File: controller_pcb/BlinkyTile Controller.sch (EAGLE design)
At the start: 29 parts, among them CON1 USB_MICROSMT+THRUHULE, Q1 16MHz, U1 MK20D--VFM5, U2 W25Q--DVSS(208), U3 74LVC1G17DCK, U4 74LVC1G17DCK, U5 74LVC1G17DCK, U6 TPD4S012

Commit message: Add protection diode, JST battery connector, tweak positions for manufacturability, redo silk
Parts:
- added CN1: (no value), adafruit:JST_2PIN-THM-RA
- added D1: (no value), adafruit:DIODESOD-323F
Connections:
- new net N$9: D1.A, L3.P$1
- net +5V: now also CN1.2, D1.C; no longer L3.P$1
- net GND: now also CN1.1
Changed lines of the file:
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@@
 <part name="L3" library="blinkinlabs" deviceset="FB" device="0805/NO-OUTLINE" value="130ohm @100MHz"/>
 <part name="L2" library="blinkinlabs" deviceset="FB" device="0805/NO-OUTLINE" value="130ohm @100MHz"/>
+<part name="CN1" library="adafruit" deviceset="JST_2PIN" device="-THM-RA"/>
+<part name="P+5" library="supply1" deviceset="+5V" device=""/>
+<part name="GND6" library="supply1" deviceset="GND" device=""/>
+<part name="D1" library="adafruit" deviceset="DIODE" device="SOD-323F"/>
 </parts>
 <sheets>
@@
 <instance part="L3" gate="G$1" x="78.74" y="195.58"/>
 <instance part="L2" gate="G$1" x="43.18" y="172.72" rot="R90"/>
+<instance part="CN1" gate="G$1" x="50.8" y="119.38" rot="R180"/>
+<instance part="P+5" gate="1" x="60.96" y="127" smashed="yes">
+<attribute name="VALUE" x="58.42" y="128.27" size="1.778" layer="96"/>
+</instance>
+<instance part="GND6" gate="1" x="60.96" y="109.22"/>
+<instance part="D1" gate="G$1" x="91.44" y="195.58"/>
 </instances>
 <busses>
@@
 <wire x1="43.18" y1="38.1" x2="43.18" y2="40.64" width="0.1524" layer="91"/>
 <junction x="48.26" y="38.1"/>
+</segment>
+<segment>
+<pinref part="CN1" gate="G$1" pin="1"/>
+<pinref part="GND6" gate="1" pin="GND"/>
+<wire x1="53.34" y1="116.84" x2="60.96" y2="116.84" width="0.1524" layer="91"/>
+<wire x1="60.96" y1="116.84" x2="60.96" y2="111.76" width="0.1524" layer="91"/>
 </segment>
 </net>
@@
 <pinref part="C8" gate="G$1" pin="1"/>
 <wire x1="116.84" y1="215.9" x2="116.84" y2="218.44" width="0.1524" layer="91"/>
-<pinref part="L3" gate="G$1" pin="P$1"/>
-<wire x1="101.6" y1="195.58" x2="83.82" y2="195.58" width="0.1524" layer="91"/>
+<wire x1="101.6" y1="195.58" x2="93.98" y2="195.58" width="0.1524" layer="91"/>
+<pinref part="D1" gate="G$1" pin="C"/>
 </segment>
 <segment>
@@
 <pinref part="U3" gate="G$2" pin="VCC"/>
 <wire x1="132.08" y1="76.2" x2="132.08" y2="73.66" width="0.1524" layer="91"/>
+</segment>
+<segment>
+<pinref part="CN1" gate="G$1" pin="2"/>
+<wire x1="53.34" y1="119.38" x2="60.96" y2="119.38" width="0.1524" layer="91"/>
+<pinref part="P+5" gate="1" pin="+5V"/>
+<wire x1="60.96" y1="119.38" x2="60.96" y2="124.46" width="0.1524" layer="91"/>
 </segment>
 </net>
@@
 </segment>
 </net>
+<net name="N$9" class="0">
+<segment>
+<pinref part="L3" gate="G$1" pin="P$1"/>
+<pinref part="D1" gate="G$1" pin="A"/>
+<wire x1="88.9" y1="195.58" x2="83.82" y2="195.58" width="0.1524" layer="91"/>
+</segment>
+</net>

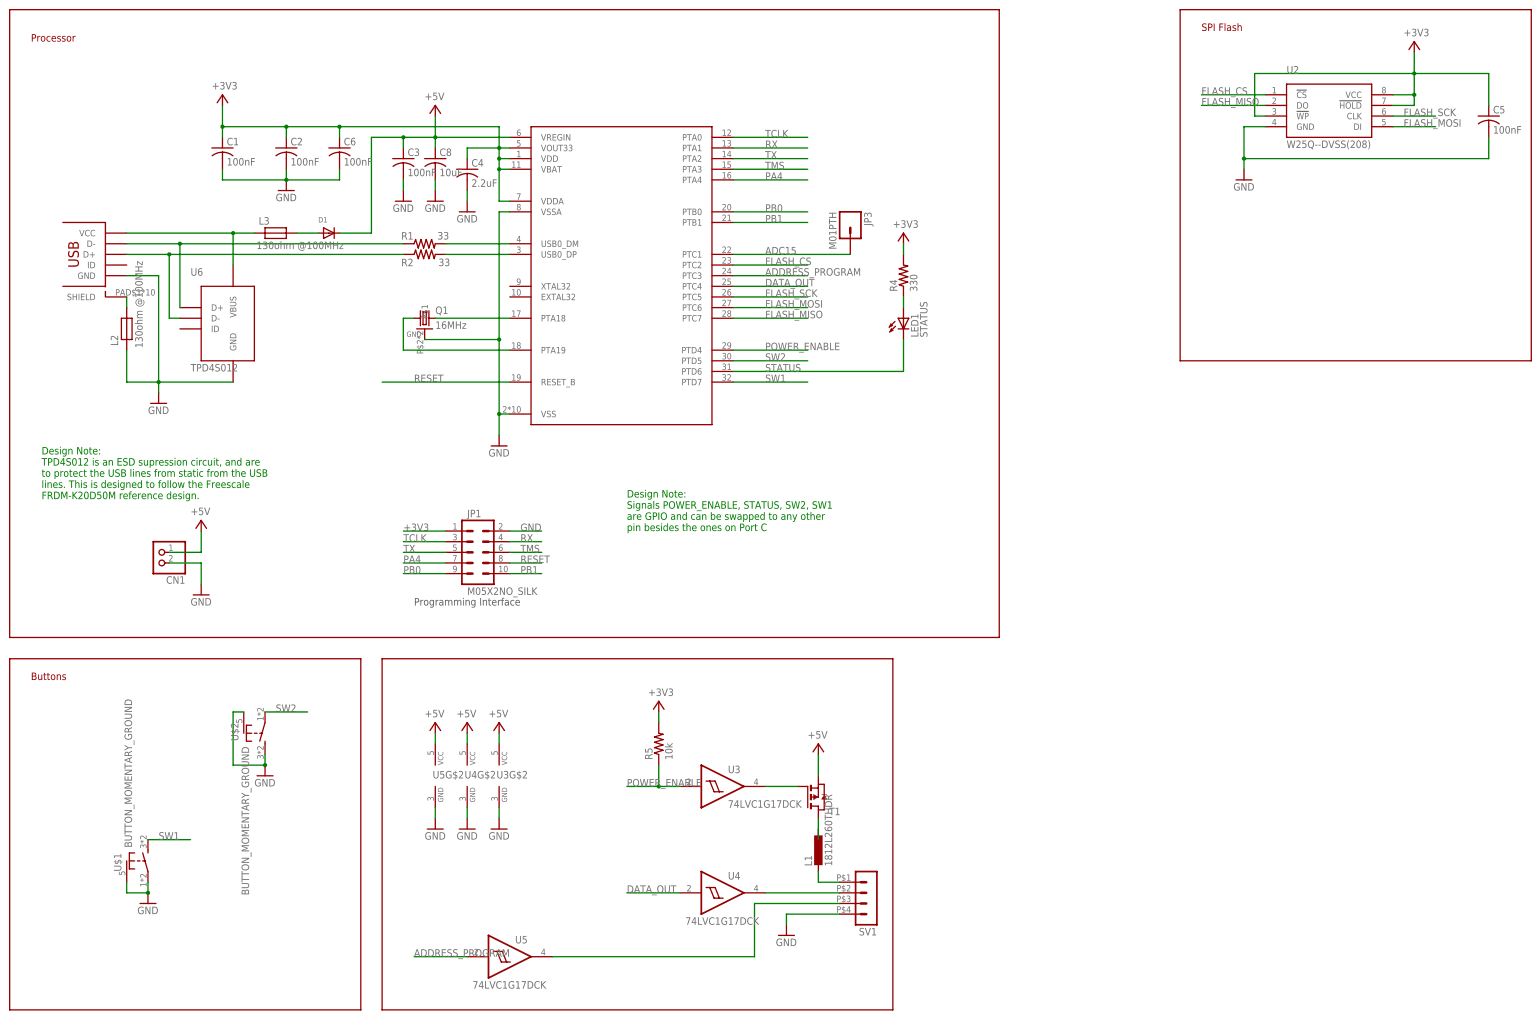
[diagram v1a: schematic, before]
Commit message: Clean up schematic layout
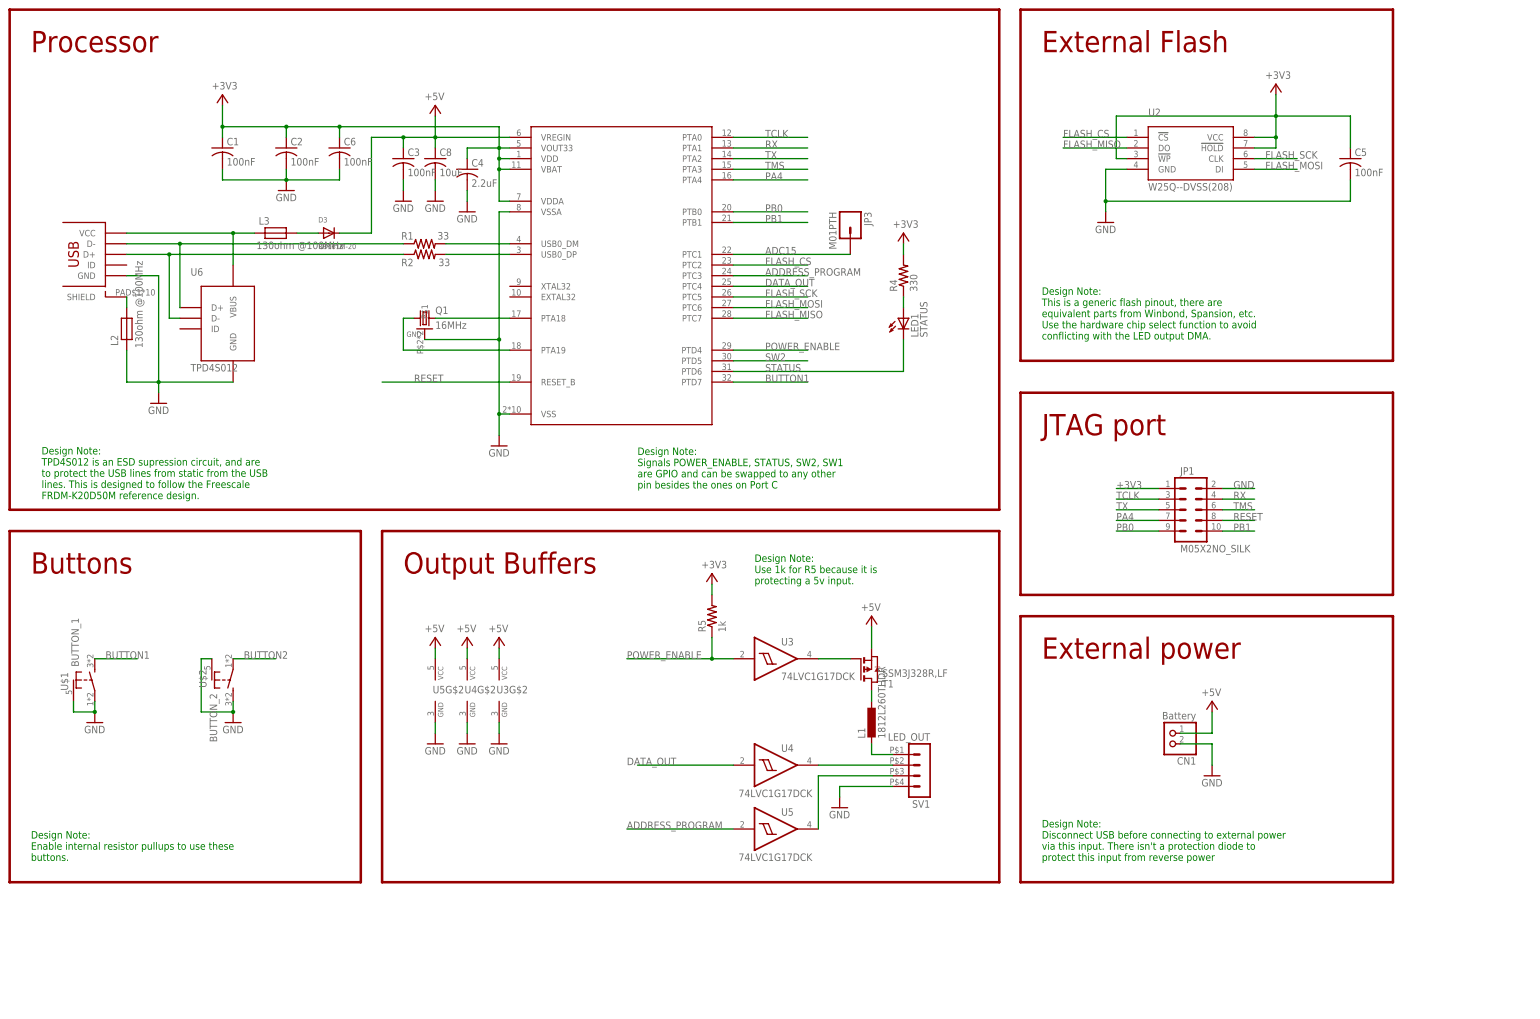
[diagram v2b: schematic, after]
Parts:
- removed D1: (no value), adafruit:DIODESOD-323F
- added D3: RB161M-20, adafruit:DIODESOD-123
- CN1: value (none) -> Battery
- R5: value 10k -> 1k
- SV1: value (none) -> LED_OUT
- T1: value (none) -> SSM3J328R,LF
- U$1: value BUTTON_MOMENTARY_GROUND -> BUTTON_1
- U$2: value BUTTON_MOMENTARY_GROUND -> BUTTON_2
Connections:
- net SW1 renamed BUTTON1
- new net BUTTON2: U$2.P
- net +5V: now also D3.C; no longer D1.C
- net N$9: now also D3.A; no longer D1.A
- net SW2: no longer U$2.P
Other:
- note added: "Design Note: Disconnect USB before connecting to external power via this input. There isn't a protection diode to protect this input from reverse power"
- note added: "Design Note: Enable internal resistor pullups to use these buttons."
- note added: "Design Note: This is a generic flash pinout, there are equivalent parts from Winbond, Spansion, etc. Use the hardware chip select function to avoid conflicting with the LED output DMA."
- note added: "Design Note: Use 1k for R5 because it is protecting a 5v input."
- note added: "External Flash"
- note added: "External power"
- note added: "JTAG port"
- note added: "Output Buffers"
- note removed: "Programming Interface"
- note removed: "SPI Flash"
- moved on the sheet: C5, CN1, JP1, L1, R5, SV1, T1, U$1, U$2, U2, U3, U3G$2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

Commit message: Controller boar design, as released.
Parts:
- R4: value 330 -> 470
- renumbered D3 to D1, JP1 to CON2, JP3 to CON4, SV1 to CON3, U$1 to SW1, U$2 to SW2
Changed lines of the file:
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@@
 <part name="FRAME1" library="frames" deviceset="DINA3_L" device=""/>
 <part name="C1" library="adafruit" deviceset="C-US" device="C0402" value="100nF"/>
-<part name="R4" library="adafruit" deviceset="R-US_" device="R0402" value="330"/>
+<part name="R4" library="adafruit" deviceset="R-US_" device="R0402" value="470"/>
 <part name="LED1" library="adafruit" deviceset="LED" device="CHIPLED_0805" value="STATUS"/>
 <part name="GND12" library="supply1" deviceset="GND" device=""/>
@@
 <part name="C6" library="adafruit" deviceset="C-US" device="C0402" value="100nF"/>
 <part name="R5" library="adafruit" deviceset="R-US_" device="R0402" value="1k"/>
-<part name="SV1" library="blinkinlabs" deviceset="4-PIN_DUPONT" device="" value="LED_OUT"/>
+<part name="CON3" library="blinkinlabs" deviceset="4-PIN_DUPONT" device="" value="LED_OUT"/>
 <part name="C8" library="adafruit" deviceset="C-US" device="C0805K" value="10uF"/>
 <part name="GND11" library="supply1" deviceset="GND" device=""/>
 <part name="3V4" library="supply1" deviceset="+3V3" device=""/>
-<part name="JP1" library="SparkFun-Connectors" deviceset="M05X2" device="NO_SILK"/>
-<part name="JP3" library="SparkFun-Connectors" deviceset="M01" device="PTH"/>
-<part name="U$1" library="blinkinlabs" deviceset="BUTTON_MOMENTARY_GROUND" device="" value="BUTTON_1"/>
-<part name="U$2" library="blinkinlabs" deviceset="BUTTON_MOMENTARY_GROUND" device="" value="BUTTON_2"/>
+<part name="CON2" library="SparkFun-Connectors" deviceset="M05X2" device="NO_SILK"/>
+<part name="CON4" library="SparkFun-Connectors" deviceset="M01" device="PTH"/>
+<part name="SW1" library="blinkinlabs" deviceset="BUTTON_MOMENTARY_GROUND" device="" value="BUTTON_1"/>
+<part name="SW2" library="blinkinlabs" deviceset="BUTTON_MOMENTARY_GROUND" device="" value="BUTTON_2"/>
 <part name="U6" library="blinkinlabs" deviceset="TPD4S012" device=""/>
 <part name="L3" library="blinkinlabs" deviceset="FB" device="0805/NO-OUTLINE" value="130ohm @100MHz"/>
@@
 <part name="P+5" library="supply1" deviceset="+5V" device=""/>
 <part name="GND6" library="supply1" deviceset="GND" device=""/>
-<part name="D3" library="adafruit" deviceset="DIODE" device="SOD-123" value="RB161M-20"/>
+<part name="D1" library="adafruit" deviceset="DIODE" device="SOD-123" value="RB161M-20"/>
 </parts>
 <sheets>
@@
 <instance part="C6" gate="G$1" x="93.98" y="215.9"/>
 <instance part="R5" gate="G$1" x="182.88" y="104.14" rot="R90"/>
-<instance part="SV1" gate="1" x="233.68" y="66.04" rot="R180"/>
+<instance part="CON3" gate="1" x="233.68" y="66.04" rot="R180"/>
 <instance part="C8" gate="G$1" x="116.84" y="213.36"/>
 <instance part="GND11" gate="1" x="116.84" y="203.2"/>
@@
 <attribute name="VALUE" x="180.34" y="115.57" size="1.778" layer="96"/>
 </instance>
-<instance part="JP1" gate="G$1" x="297.18" y="129.54"/>
-<instance part="JP3" gate="G$1" x="215.9" y="198.12" rot="R270"/>
-<instance part="U$1" gate="G$1" x="33.02" y="88.9" smashed="yes">
+<instance part="CON2" gate="G$1" x="297.18" y="129.54"/>
+<instance part="CON4" gate="G$1" x="215.9" y="198.12" rot="R270"/>
+<instance part="SW1" gate="G$1" x="33.02" y="88.9" smashed="yes">
 <attribute name="NAME" x="29.21" y="86.36" size="1.778" layer="95" rot="R90"/>
 <attribute name="VALUE" x="31.75" y="92.075" size="1.778" layer="96" rot="R90"/>
 </instance>
-<instance part="U$2" gate="G$1" x="66.04" y="88.9" smashed="yes" rot="MR180">
+<instance part="SW2" gate="G$1" x="66.04" y="88.9" smashed="yes" rot="MR180">
 <attribute name="NAME" x="62.23" y="91.44" size="1.778" layer="95" rot="MR270"/>
 <attribute name="VALUE" x="64.77" y="85.725" size="1.778" layer="96" rot="MR270"/>
@@
 </instance>
 <instance part="GND6" gate="1" x="302.26" y="66.04"/>
-<instance part="D3" gate="G$1" x="91.44" y="195.58"/>
+<instance part="D1" gate="G$1" x="91.44" y="195.58"/>
 </instances>
 <busses>
@@
 <wire x1="213.36" y1="60.96" x2="213.36" y2="63.5" width="0.1524" layer="91"/>
 <wire x1="213.36" y1="63.5" x2="226.06" y2="63.5" width="0.1524" layer="91"/>
-<pinref part="SV1" gate="1" pin="4"/>
+<pinref part="CON3" gate="1" pin="4"/>
 </segment>
 <segment>
@@
 <wire x1="304.8" y1="134.62" x2="312.42" y2="134.62" width="0.1524" layer="91"/>
 <label x="307.34" y="134.62" size="1.778" layer="95"/>
-<pinref part="JP1" gate="G$1" pin="2"/>
+<pinref part="CON2" gate="G$1" pin="2"/>
 </segment>
 <segment>
@@
 <segment>
 <pinref part="GND2" gate="1" pin="GND"/>
-<pinref part="U$2" gate="G$1" pin="S"/>
+<pinref part="SW2" gate="G$1" pin="S"/>
 <wire x1="68.58" y1="83.82" x2="68.58" y2="81.28" width="0.1524" layer="91"/>
-<pinref part="U$2" gate="G$1" pin="SHIELD"/>
+<pinref part="SW2" gate="G$1" pin="SHIELD"/>
 <wire x1="63.5" y1="93.98" x2="60.96" y2="93.98" width="0.1524" layer="91"/>
 <wire x1="60.96" y1="93.98" x2="60.96" y2="81.28" width="0.1524" layer="91"/>
@@
 </segment>
 <segment>
-<pinref part="U$1" gate="G$1" pin="P"/>
+<pinref part="SW1" gate="G$1" pin="P"/>
 <pinref part="GND12" gate="1" pin="GND"/>
 <wire x1="35.56" y1="83.82" x2="35.56" y2="81.28" width="0.1524" layer="91"/>
 <wire x1="35.56" y1="81.28" x2="30.48" y2="81.28" width="0.1524" layer="91"/>
-<pinref part="U$1" gate="G$1" pin="SHIELD"/>
+<pinref part="SW1" gate="G$1" pin="SHIELD"/>
 <wire x1="30.48" y1="81.28" x2="30.48" y2="83.82" width="0.1524" layer="91"/>
 <junction x="35.56" y="81.28"/>
@@
 <wire x1="116.84" y1="215.9" x2="116.84" y2="218.44" width="0.1524" layer="91"/>
 <wire x1="101.6" y1="195.58" x2="93.98" y2="195.58" width="0.1524" layer="91"/>
-<pinref part="D3" gate="G$1" pin="C"/>
+<pinref part="D1" gate="G$1" pin="C"/>
 </segment>
 <segment>
@@
 <wire x1="289.56" y1="134.62" x2="279.4" y2="134.62" width="0.1524" layer="91"/>
 <label x="279.4" y="134.62" size="1.778" layer="95"/>
-<pinref part="JP1" gate="G$1" pin="1"/>
+<pinref part="CON2" gate="G$1" pin="1"/>
 </segment>
 <segment>
@@
 <wire x1="289.56" y1="132.08" x2="279.4" y2="132.08" width="0.1524" layer="91"/>
 <label x="279.4" y="132.08" size="1.778" layer="95"/>
-<pinref part="JP1" gate="G$1" pin="3"/>
+<pinref part="CON2" gate="G$1" pin="3"/>
 </segment>
 <segment>
@@
 <wire x1="304.8" y1="129.54" x2="312.42" y2="129.54" width="0.1524" layer="91"/>
 <label x="307.34" y="129.54" size="1.778" layer="95"/>
-<pinref part="JP1" gate="G$1" pin="6"/>
+<pinref part="CON2" gate="G$1" pin="6"/>
 </segment>
 </net>
@@
 <wire x1="312.42" y1="132.08" x2="304.8" y2="132.08" width="0.1524" layer="91"/>
 <label x="307.34" y="132.08" size="1.778" layer="95"/>
-<pinref part="JP1" gate="G$1" pin="4"/>
+<pinref part="CON2" gate="G$1" pin="4"/>
 </segment>
 </net>
@@
 <wire x1="289.56" y1="129.54" x2="279.4" y2="129.54" width="0.1524" layer="91"/>
 <label x="279.4" y="129.54" size="1.778" layer="95"/>
-<pinref part="JP1" gate="G$1" pin="5"/>
+<pinref part="CON2" gate="G$1" pin="5"/>
 </segment>
 </net>
@@
 <wire x1="304.8" y1="127" x2="312.42" y2="127" width="0.1524" layer="91"/>
 <label x="307.34" y="127" size="1.778" layer="95"/>
-<pinref part="JP1" gate="G$1" pin="8"/>
+<pinref part="CON2" gate="G$1" pin="8"/>
 </segment>
 </net>
@@
 <wire x1="35.56" y1="93.98" x2="45.72" y2="93.98" width="0.1524" layer="91"/>
 <label x="38.1" y="93.98" size="1.778" layer="95"/>
-<pinref part="U$1" gate="G$1" pin="S"/>
+<pinref part="SW1" gate="G$1" pin="S"/>
 </segment>
 <segment>
@@
 <pinref part="U4" gate="G$1" pin="O"/>
 <wire x1="208.28" y1="68.58" x2="226.06" y2="68.58" width="0.1524" layer="91"/>
-<pinref part="SV1" gate="1" pin="2"/>
+<pinref part="CON3" gate="1" pin="2"/>
 </segment>
 </net>
@@
 <segment>
 <pinref part="U5" gate="G$1" pin="O"/>
-<pinref part="SV1" gate="1" pin="3"/>
+<pinref part="CON3" gate="1" pin="3"/>
 <wire x1="226.06" y1="66.04" x2="208.28" y2="66.04" width="0.1524" layer="91"/>
 <wire x1="208.28" y1="66.04" x2="208.28" y2="53.34" width="0.1524" layer="91"/>
@@
 <wire x1="187.96" y1="190.5" x2="215.9" y2="190.5" width="0.1524" layer="91"/>
 <label x="195.58" y="190.5" size="1.778" layer="95"/>
-<pinref part="JP3" gate="G$1" pin="1"/>
+<pinref part="CON4" gate="G$1" pin="1"/>
 </segment>
 </net>
@@
 <wire x1="289.56" y1="127" x2="279.4" y2="127" width="0.1524" layer="91"/>
 <label x="279.4" y="127" size="1.778" layer="95"/>
-<pinref part="JP1" gate="G$1" pin="7"/>
+<pinref part="CON2" gate="G$1" pin="7"/>
 </segment>
 </net>
@@
 <wire x1="289.56" y1="124.46" x2="279.4" y2="124.46" width="0.1524" layer="91"/>
 <label x="279.4" y="124.46" size="1.778" layer="95"/>
-<pinref part="JP1" gate="G$1" pin="9"/>
+<pinref part="CON2" gate="G$1" pin="9"/>
 </segment>
 </net>
@@
 <wire x1="304.8" y1="124.46" x2="312.42" y2="124.46" width="0.1524" layer="91"/>
 <label x="307.34" y="124.46" size="1.778" layer="95"/>
-<pinref part="JP1" gate="G$1" pin="10"/>
+<pinref part="CON2" gate="G$1" pin="10"/>
 </segment>
 </net>
@@
 <net name="N$8" class="0">
 <segment>
-<pinref part="SV1" gate="1" pin="1"/>
+<pinref part="CON3" gate="1" pin="1"/>
 <wire x1="226.06" y1="71.12" x2="220.98" y2="71.12" width="0.1524" layer="91"/>
 <wire x1="220.98" y1="71.12" x2="220.98" y2="73.66" width="0.1524" layer="91"/>
@@
 <pinref part="L3" gate="G$1" pin="P$1"/>
 <wire x1="88.9" y1="195.58" x2="83.82" y2="195.58" width="0.1524" layer="91"/>
-<pinref part="D3" gate="G$1" pin="A"/>
+<pinref part="D1" gate="G$1" pin="A"/>
 </segment>
 </net>
@@
 <segment>
 <label x="71.12" y="93.98" size="1.778" layer="95"/>
-<pinref part="U$2" gate="G$1" pin="P"/>
+<pinref part="SW2" gate="G$1" pin="P"/>
 <wire x1="68.58" y1="93.98" x2="78.74" y2="93.98" width="0.1524" layer="91"/>
 </segment>

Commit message: Controller pcb, as fixed
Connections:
- removed net SW2: U1.PTD5
- net BUTTON2: now also U1.PTD5
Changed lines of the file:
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@@
-</segment>
-</net>
-<net name="SW2" class="0">
-<segment>
-<pinref part="U1" gate="G$1" pin="PTD5"/>
-<wire x1="187.96" y1="165.1" x2="205.74" y2="165.1" width="0.1524" layer="91"/>
-<label x="195.58" y="165.1" size="1.778" layer="95"/>
 </segment>
 </net>
@@
 <wire x1="68.58" y1="93.98" x2="78.74" y2="93.98" width="0.1524" layer="91"/>
 </segment>
+<segment>
+<pinref part="U1" gate="G$1" pin="PTD5"/>
+<wire x1="187.96" y1="165.1" x2="205.74" y2="165.1" width="0.1524" layer="91"/>
+<label x="195.58" y="165.1" size="1.778" layer="95"/>
+</segment>
 </net>

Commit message: Update note about board
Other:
- note added: "Design Note: Use the hardware chip select function to avoid GPIO write conflicts with the LED output DMA. Part number is generic, use: S25FL216K0PMFI011"
- note removed: "Design Note: This is a generic flash pinout, there are equivalent parts from Winbond, Spansion, etc. Use the hardware chip select function to avoid conflicting with the LED output DMA."
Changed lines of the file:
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@@
 <?xml version="1.0" encoding="utf-8"?>
 <!DOCTYPE eagle SYSTEM "eagle.dtd">
-<eagle version="7.2.0">
+<eagle version="7.7.0">
 <drawing>
 <settings>
@@
 protecting a 5v input.</text>
 <text x="261.62" y="170.18" size="1.778" layer="91">Design Note:
-This is a generic flash pinout, there are
-equivalent parts from Winbond, Spansion, etc.
 Use the hardware chip select function to avoid
-conflicting with the LED output DMA.</text>
+GPIO write conflicts with the LED output DMA.
+Part number is generic, use:
+S25FL216K0PMFI011</text>
 <text x="261.62" y="45.72" size="1.778" layer="91">Design Note:
 Disconnect USB before connecting to external power
